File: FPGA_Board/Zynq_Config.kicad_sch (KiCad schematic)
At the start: 1 part

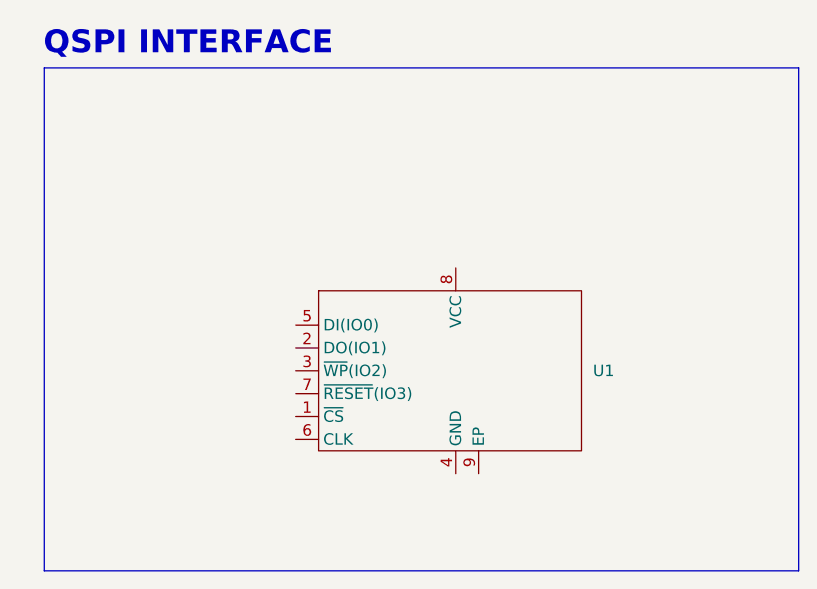
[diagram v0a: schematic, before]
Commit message: Create Block Diagram, create Vivado Project
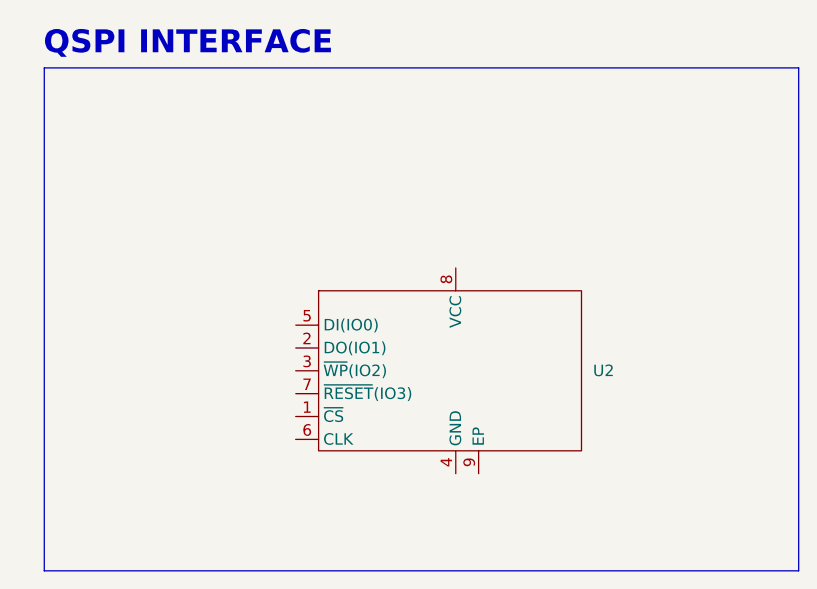
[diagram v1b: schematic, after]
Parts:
- renumbered U1 to U2
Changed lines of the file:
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@@
 		(dnp no)
 		(fields_autoplaced yes)
-		(property "Reference" "U1"
+		(property "Reference" "U2"
 			(at 88.9 161.2899 0)
 			(effects
@@
 		(instances
 			(project "FPGA_Board"
-				(path "/472f09b1-9eb3-4828-aa92-3f9176530a4e/1202234b-3398-4b70-bea7-fa7b5bc7f21a"
-					(reference "U1")
+				(path "/472f09b1-9eb3-4828-aa92-3f9176530a4e/a09a964b-ed9f-455d-a2b6-3b3670da4e94"
+					(reference "U2")
 					(unit 1)
 				)

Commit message: - modify USB connector design in FPGA Board
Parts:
- U2: value ~ -> (none)
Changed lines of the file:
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@@
 (kicad_sch
-	(version 20250114)
+	(version 20260306)
 	(generator "eeschema")
-	(generator_version "9.0")
+	(generator_version "10.0")
 	(paper "A4")
 	(title_block
@@
 		(at 72.39 161.29 0)
 		(unit 1)
+		(body_style 1)
 		(exclude_from_sim no)
 		(in_bom yes)
 		(on_board yes)
+		(in_pos_files yes)
 		(dnp no)
 		(fields_autoplaced yes)
 		(property "Reference" "U2"
 			(at 88.9 161.2899 0)
+			(show_name no)
+			(do_not_autoplace no)
 			(effects
 				(font
@@
 			)
 		)
-		(property "Value" "~"
+		(property "Value" ""
 			(at 72.39 161.29 0)
+			(hide yes)
+			(show_name no)
+			(do_not_autoplace no)
 			(effects
 				(font
 					(size 1.27 1.27)
 				)
-				(hide yes)
 			)
 		)
 		(property "Footprint" "Package_SON:WSON-8-1EP_8x6mm_P1.27mm_EP3.4x4.3mm"
 			(at 67.056 144.018 0)
+			(hide yes)
+			(show_name no)
+			(do_not_autoplace no)
 			(effects
 				(font
 					(size 1.27 1.27)
 				)
-				(hide yes)
 			)
 		)
 		(property "Datasheet" "https://www.winbond.com/resource-files/w25q128jv%20revf%2003272018%20plus.pdf"
 			(at 72.39 161.29 0)
+			(hide yes)
+			(show_name no)
+			(do_not_autoplace no)
 			(effects
 				(font
 					(size 1.27 1.27)
 				)
-				(hide yes)
 			)
 		)
 		(property "Description" "NOR Flash spiFlash, 3V, 128M-bit, 4Kb Uniform Sector"
 			(at 66.04 141.224 0)
+			(hide yes)
+			(show_name no)
+			(do_not_autoplace no)
 			(effects
 				(font
 					(size 1.27 1.27)
 				)
-				(hide yes)
 			)
 		)
